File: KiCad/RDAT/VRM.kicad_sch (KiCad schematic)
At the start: 52 parts, among them U6 BQ24617RGER

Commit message: added volage stuffs
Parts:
- removed C33, C36, C43: 1uF, symbol Device:C_Polarized_Small_US
- removed C34, C35, C37, C38, C39: 0.1uF, symbol Device:C_Small
- removed C40, C41: 10uF, symbol Device:C_Small
- removed C42: 22pF, symbol Device:C_Small
- removed C44, C47, C48: 1uF, symbol Device:C_Small
- removed C45, C46: 10uF, symbol Device:C_Polarized_Small_US
- removed C49: 2.2uF, symbol Device:C_Polarized_Small_US
- removed CTTC1: 0.056uF, symbol Device:C_Polarized_Small_US
- removed D111: BAT54J, Diode_SMD:D_SOD-323F, symbol Diode:BAT54J
- removed D112, D113, D114: LED, symbol Device:LED
- removed L1: 6.8uH, symbol Device:L_Small
- removed MOSFET2, MOSFET4: SIS412DN-T1-GE3, POWERPAK_1212-8, symbol SIS412DN:SIS412DN-T1-GE3
- removed MOSFET3, MOSFET5, MOSFET6: SI7617DN-T1-GE3, POWERPAK_1212-8_VIS, symbol SI7617DN-T1-GE3:SI7617DN-T1-GE3
- removed R31: 9.31k, symbol Device:R_Small_US
- removed R32: 100, symbol Device:R_Small_US
- removed R33: 430, symbol Device:R_Small_US
- removed R34: 22k, symbol Device:R_Small_US
- removed R35: 82k, symbol Device:R_Small_US
- removed R36: 36k, symbol Device:R_Small_US
- removed R37, R38, R39, R44, R45, R46, R47: 10k, symbol Device:R_Small_US
- removed R40, R51: 100k, symbol Device:R_Small_US
- removed R41, R52: 1k, symbol Device:R_Small_US
- removed R43: 70k, symbol Device:R_Small_US
- removed R48: 10, symbol Device:R_Small_US
- removed R50: 2, symbol Device:R_Small_US
- removed R_{AC}: 0.02, symbol Device:R_Small_US
- removed R_{SR}: 0.028, symbol Device:R_Small_US
- removed TH2: 103AT, symbol Device:Thermistor_US
- removed U6: BQ24617RGER, RGE24_2P45X2P45, symbol BQ24617RGER:BQ24617RGER
- added L2: L, symbol Device:L
- added R42, R49: R_Small_US, symbol Device:R_Small_US
- added U7, U8, U9: TPS54331DR, D8, symbol TPS54331DR:TPS54331DR
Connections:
- net GND: now also R42.1, U7.7 (GND), U8.7 (GND), U9.7 (GND)
- new net: L2.1, U7.8 (PH)
- new net +10V: L2.2, R49.2
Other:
- note removed: "Q1"
- note removed: "Q2"

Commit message: Update VRM stuff
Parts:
- removed L2: L, symbol Device:L
- added C51, C52, C53, C54, C55, C56, C57, C58, C59, C60, C61, C62, C63, C64, C65, C66, C67, C68, C69, C70, C71, C74, C75, C76, C77: C_Small, symbol Device:C_Small
- added C72: 12.5nF, symbol Device:C_Small
- added C73: 0.1uF, symbol Device:C_Small
- added D115, D116, D117: B340, Diode_SMD:D_SMC, symbol Diode:B340
- added D118, D119, D120, D121, D122, D123: D_Schottky, symbol Device:D_Schottky
- added L2, L3, L4: L_Iron, symbol Device:L_Iron
- added R53, R61, R67: 0, symbol Device:R_Small_US
- added R54, R55, R56, R57, R58, R59, R60, R62, R65, R66, R68: R_Small_US, symbol Device:R_Small_US
- added R63: 680k, symbol Device:R_Small_US
- added R64: 75k, symbol Device:R_Small_US
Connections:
- net +10V: now also C52.1, C53.1, L2.2, R53.2; no longer R49.2
- net +3V3: now also C76.1, C77.1, L4.2, R67.2
- net +5V: now also C67.1, C68.1, L3.2, R61.2
- net GND: now also C52.2, C53.2, C54.2, C56.2, C57.2, C58.2, C59.2, C60.2, C61.2, C62.2, C63.2, C65.2, C67.2, C68.2, C69.2, C70.2, C71.2, C72.2, C74.2, C76.2, C77.2, D115.2 (A), D116.2 (A), D117.2 (A), R54.1, R55.1, R58.1, R59.1, R60.1, R64.1, R65.1, R66.1
- net at U7.8 (PH): now also C51.1, D115.1 (K), L2.1
- net at R42.2: now also R49.1, U7.5 (VSENSE)
- net at U7.1 (BOOT): now also C51.2
- net voltIn: now reaches U7.2 (VIN)
- net voltIn: now also U8.2 (VIN), U9.2 (VIN), C57.1, C58.1, C59.1, C60.1, C61.1, C62.1, C69.1, C70.1, C71.1, D118.1 (K), D119.1 (K), D120.1 (K), D121.1 (K), D122.1 (K), D123.1 (K), R56.2, R57.2, R63.2
- net at U7.3 (EN): now also R55.2, R56.1
- net at U7.4 (SS): now also C56.1
- net at U7.6 (COMP): now also C54.1, C55.1
- net at U8.1 (BOOT): now also C64.2
- net at U8.3 (EN): now also R57.1, R58.2
- net at U8.4 (SS): now also C63.1
- net at U8.5 (VSENSE): now also R60.2, R62.1
- net at U8.6 (COMP): now also C65.1, C66.1
- net at U8.8 (PH): now also C64.1, D116.1 (K), L3.1
- net at U9.1 (BOOT): now also C73.2
- net at U9.3 (EN): now also R63.1, R64.2
- net at U9.4 (SS): now also C72.1
- net at U9.5 (VSENSE): now also R66.2, R68.1
- net at U9.6 (COMP): now also C74.1, C75.1
- net at U9.8 (PH): now also C73.1, D117.1 (K), L4.1
- new net: R61.1, R62.2
- new net: C66.2, R59.2
- new net: C55.2, R54.2
- new net: R67.1, R68.2
- new net: R49.2, R53.1
- new net: C75.2, R65.2
- new net BatteryIn: D118.2 (A), D119.2 (A), D120.2 (A)
- new net USBPowIn: D121.2 (A), D122.2 (A), D123.2 (A)
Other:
- note added: "Swithcing Freq 570kHz"

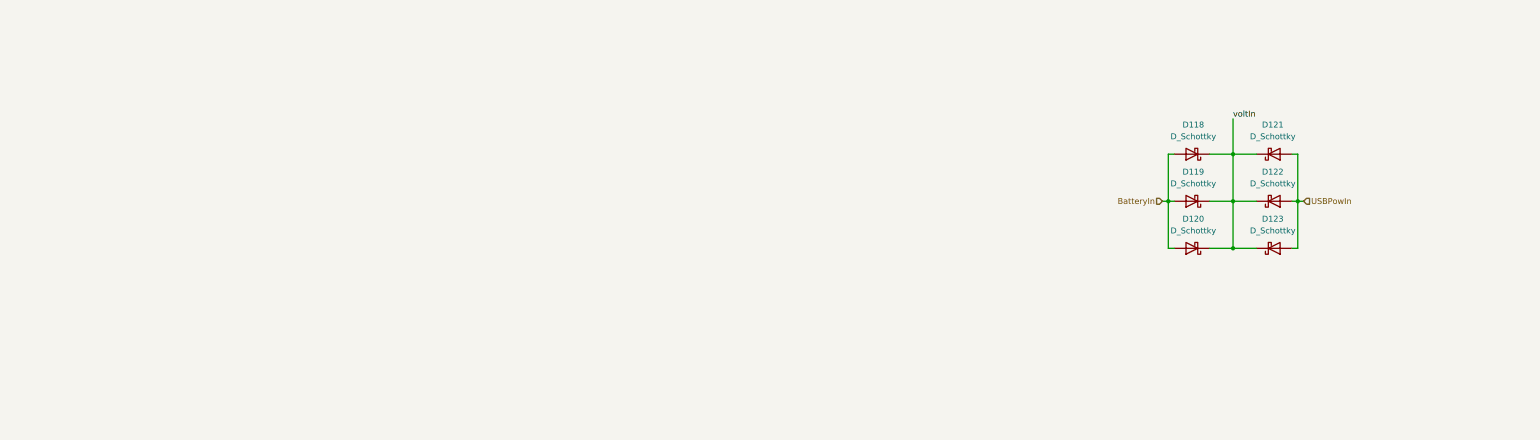
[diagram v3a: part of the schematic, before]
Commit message: Modified Power Stages
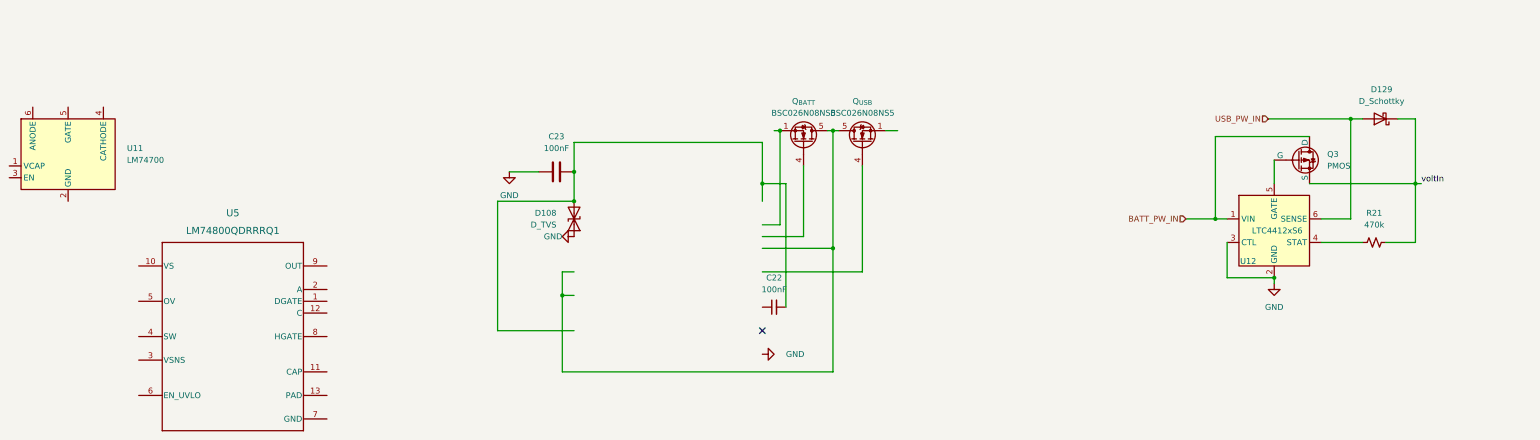
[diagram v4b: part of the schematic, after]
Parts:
- removed D118, D119, D120, D121, D122, D123: D_Schottky, symbol Device:D_Schottky
- added C22: 100nF, symbol Device:C_Small
- added C23: 100nF, symbol Device:C
- added D108: D_TVS, symbol Device:D_TVS
- added D129: D_Schottky, symbol Device:D_Schottky
- added Q3: PMOS, symbol Simulation_SPICE:PMOS
- added Q_{BATT}, Q_{USB}: BSC026N08NS5, Package_TO_SOT_SMD:TDSON-8-1, symbol Transistor_FET:BSC026N08NS5
- added R21: 470k, symbol Device:R_Small_US
- added U11: LM74700, Package_TO_SOT_SMD:SOT-23-6, symbol Power_Management:LM74700
- added U12: LTC4412xS6, Package_TO_SOT_SMD:TSOT-23-6, symbol Power_Management:LTC4412xS6
- added U5: LM74800QDRRRQ1, DRR0012E, symbol LM74800QDRRRQ1:LM74800QDRRRQ1
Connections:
- net GND: now also C23.1, D108.1 (A1), U12.2 (GND), U12.3 (CTL)
- net voltIn: now also D129.1 (K), Q3.3 (S), R21.2
- new net: Q_{BATT}.1 (S), Q_{BATT}.2 (S), Q_{BATT}.3 (S)
- new net: Q_{BATT}.5 (D), Q_{USB}.5 (D)
- new net: C22.2, C23.2, D108.2 (A2)
- new net: Q3.2 (G), U12.5 (GATE)
- new net: Q_{USB}.1 (S), Q_{USB}.2 (S), Q_{USB}.3 (S)
- new net: R21.1, U12.4 (STAT)
- new net BATT_PW_IN: Q3.1 (D), U12.1 (VIN)
- new net USB_PW_IN: D129.2 (A), U12.6 (SENSE)
- no-connect marks 0 -> 1

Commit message: Added HDMI connection and marked section for review in schematics; updated column widths in PRL file; added new operating values CSV files for power calculations.
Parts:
- removed C23: 100nF, symbol Device:C
- removed C51, C56, C57, C58, C59, C62, C63, C64, C65, C66, C67, C68, C69, C70, C71, C74, C75, C76, C77: C_Small, symbol Device:C_Small
- removed C72: 12.5nF, symbol Device:C_Small
- removed C73: 0.1uF, symbol Device:C_Small
- removed D108: D_TVS, symbol Device:D_TVS
- removed D115, D116, D117: B340, Diode_SMD:D_SMC, symbol Diode:B340
- removed L2, L3, L4: L_Iron, symbol Device:L_Iron
- removed Q_{BATT}, Q_{USB}: BSC026N08NS5, Package_TO_SOT_SMD:TDSON-8-1, symbol Transistor_FET:BSC026N08NS5
- removed R58, R59, R60, R62, R65, R66, R68: R_Small_US, symbol Device:R_Small_US
- removed R61, R67: 0, symbol Device:R_Small_US
- removed R63: 680k, symbol Device:R_Small_US
- removed R64: 75k, symbol Device:R_Small_US
- removed U11: LM74700, Package_TO_SOT_SMD:SOT-23-6, symbol Power_Management:LM74700
- removed U5: LM74800QDRRRQ1, DRR0012E, symbol LM74800QDRRRQ1:LM74800QDRRRQ1
- removed U7, U8, U9: TPS54331DR, D8, symbol TPS54331DR:TPS54331DR
- added C23: 47uF, symbol Device:C_Small
- added C32: 100nF, symbol Device:C_Small
- added C48: 33uF, symbol Device:C_Small
- added C66, C69: 1uF/16V, A_HDJ_Library:C_0402_1005Metric, symbol Device:C
- added C_{OUT}: 10uF, symbol Device:C_Small
- added Ccomp3: 1.8nF, symbol Device:C_Small
- added Cin: 4.7uF, symbol Device:C_Small
- added Css: 3.3nF, symbol Device:C_Small
- added Cvcc: 1uF, symbol Device:C_Small
- added D108, D115: ESD5V0B03, A_HDJ_Library:D_0402_1005Metric, symbol Diode:ESD9B5.0ST5G
- added D116: LED_G, A_HDJ_Library:LED_0603_1608Metric, symbol Device:LED
- added L2: 6.8uH, symbol Device:L
- added L3: 12uH, symbol Device:L
- added L4: 13uH, symbol Device:L
- added M2, M3: CSD17571Q2, DQK0006C, symbol CSD17571Q2:CSD17571Q2
- added Q8: 2N7002, A_HDJ_Library:SOT-23, symbol Transistor_FET:2N7002
- added R58, R60: 100R/1%, A_HDJ_Library:R_0402_1005Metric, symbol Device:R
- added R59, R61: 10K/1%, Resistor_SMD:R_0402_1005Metric, symbol Device:R
- added R62: 1K/1%, A_HDJ_Library:R_0402_1005Metric, symbol Device:R
- added R63: 10K/1%, A_HDJ_Library:R_0402_1005Metric, symbol Device:R
- added R64: 2.2K/1%, A_HDJ_Library:R_0402_1005Metric, symbol Device:R
- added Rcomp2: 237, symbol Device:R_Small_US
- added Rfbb: 634, symbol Device:R_Small_US
- added Rfbt: 10k, symbol Device:R_Small_US
- added SW1, SW2: SW_Push, A_HDJ_Library:SW_Push_6x6x6, symbol Switch:SW_Push
- added U5, U8: TPS54308, Package_TO_SOT_SMD:SOT-23-6, symbol Regulator_Switching:TPS54308
- added U7: TPS40345DRCR, DRC0010J, symbol TPS40345DRCR:TPS40345DRCR
- C52: value C_Small -> 270pF
- C53: value C_Small -> 12nF
- C54: value C_Small -> 470nF
- C55: value C_Small -> 100nF
- C60, C61: value C_Small -> 6.8uF
- R42: value R_Small_US -> 1.58k
- R49, R54, R56: value R_Small_US -> 100k
- R53: value 0 -> 10.2k
- R55: value R_Small_US -> 13.7k
- R57: value R_Small_US -> 22k
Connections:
- net +10V: now also C_{OUT}.2, Rfbt.2; no longer C52.1, C53.1, R53.2
- net +3V3: now also R56.1, C48.2, L4.2, R59.2, R61.2, R64.2
- net +5V: now also R54.1, C23.2, L3.2
- net GND: now also R53.1, R55.2, R57.2, C23.1, C48.1, C66.2, C69.2, C_{OUT}.1, Cin.2, Css.2, Cvcc.2, D108.1 (A1), D115.1 (A1), M2.4 (S), Q8.2 (S), R63.1, Rfbb.1, SW1.2, SW2.2, U5.1 (GND), U7.11 (PAD), U8.1 (GND); no longer C52.2, C53.2, R42.1, R54.1, R55.1
- net voltIn: now also Cin.1, Cvcc.1, M3.1 (D), M3.2 (D), U5.3 (VIN), U7.1 (VDD), U8.3 (VIN); no longer R56.2, R57.2
- net at C22.2: now also L3.1, U5.2 (SW)
- net at R57.1: now also R56.2, U8.4 (FB)
- net at R42.2: now also C52.2, Ccomp3.1, Rfbb.2, Rfbt.1, U7.5 (FB); no longer R49.1
- net at C55.2: now also L2.1, M2.1 (D), M2.2 (D), M3.4 (S), U7.8 (SW); no longer R54.2
- net at C54.1: now also R49.2, U7.10 (BP); no longer C55.1
- net at C22.1: now also U5.6 (BOOT)
- new net: C66.1, D108.2 (A2), R58.1, R59.1, SW1.1
- new net: C69.1, D115.2 (A2), R60.1, R61.1, SW2.1
- new net: Q8.1 (G), R62.2, R63.2
- new net: C52.1, C53.1, U7.4 (COMP)
- new net: M2.3 (G), R53.2, U7.9 (LDRV_OC)
- new net: D116.2 (A), R64.1
- new net: C32.2, L4.1, U8.2 (SW)
- new net: M3.3 (G), U7.7 (HDRV)
- new net: C53.2, R42.1
- new net: C55.1, U7.6 (BOOT)
- new net: R49.1, U7.3 (PGOOD)
- new net: L2.2, Rcomp2.2
- new net: R54.2, R55.1, U5.4 (FB)
- new net: D116.1 (K), Q8.3 (D)
- new net: Css.1, U7.2 (EN_SS)
- new net: Ccomp3.2, Rcomp2.1
- new net: C32.1, U8.6 (BOOT)
- new net ~{PWR_LED}/~{PSON}: R62.1
- new net ~{PWR_SW}: R58.2
- new net ~{RST_SW}: R60.2
- no-connect marks 1 -> 6
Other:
- note added: "LattePanda Mu has integrated pull-up resistors."
- note removed: "Swithcing Freq 570kHz"
- moved on the sheet: C60, D129, Q3, R21, U12

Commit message: 2x checked all schematics
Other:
- note added: "volt in always at 12-16.8v"
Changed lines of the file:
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@@
 		(rev "0")
+	)
+	(text "volt in always at 12-16.8v\n"
+		(exclude_from_sim no)
+		(at 72.898 184.912 0)
+		(effects
+			(font
+				(size 1.27 1.27)
+			)
+		)
 	)
 	(text "LattePanda Mu has integrated pull-up resistors."
